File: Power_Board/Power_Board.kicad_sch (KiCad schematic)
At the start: 7 parts, among them J1 Screw_Terminal_01x02, J1_left1 Conn_01x12_Female, J1_right1 Conn_01x12_Female, J2 Conn_01x06_Female, J3 Screw_Terminal_01x02

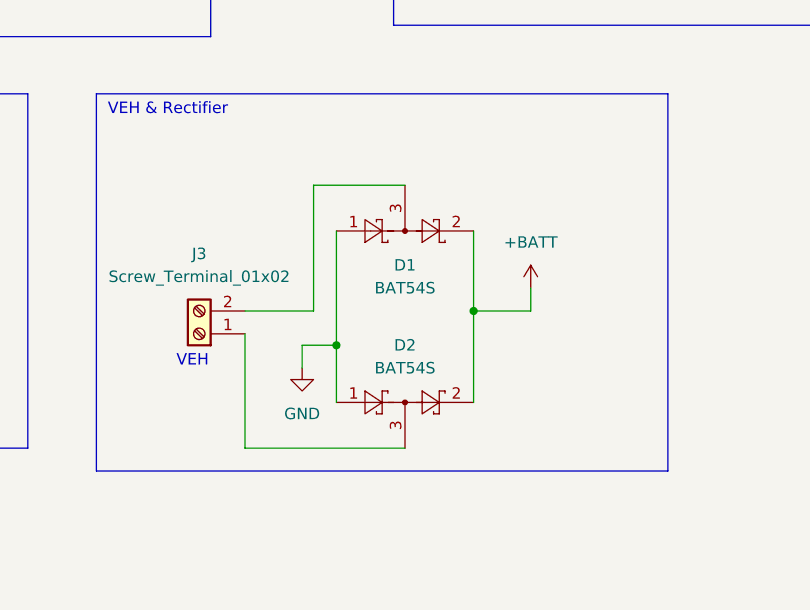
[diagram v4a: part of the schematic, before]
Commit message: Changed diod footprint
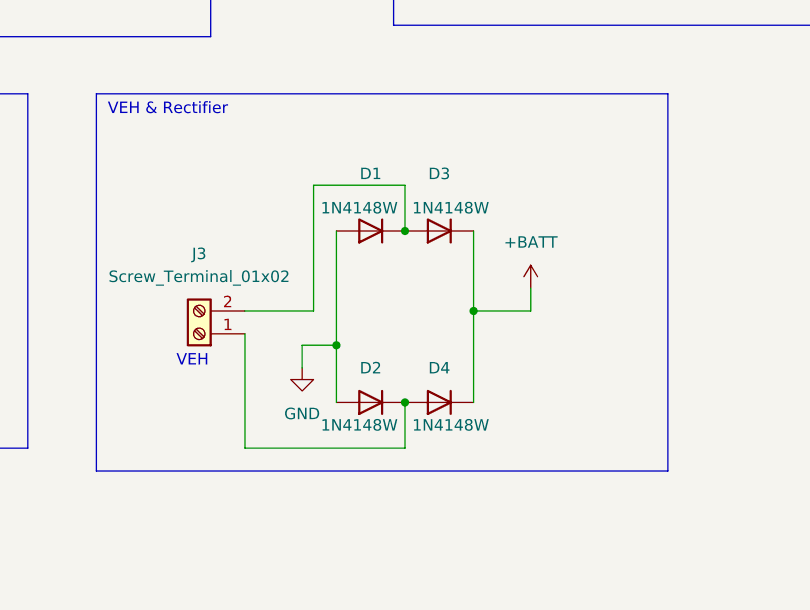
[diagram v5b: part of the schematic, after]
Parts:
- removed D1, D2: BAT54S, Package_TO_SOT_SMD:SOT-23, symbol Diode:BAT54S
- added D1, D2, D3, D4: 1N4148W, Diode_SMD:D_SOD-123, symbol Diode:1N4148W
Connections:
- net +BATT: now also D3.1 (K), D4.1 (K)
- net GND: now also D1.2 (A), D2.2 (A)
- net at J3.1 (Pin_1): now also D2.1 (K), D4.2 (A)
- net at J3.2 (Pin_2): now also D1.1 (K), D3.2 (A)
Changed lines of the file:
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@@
   (junction (at 105.41 105.41) (diameter 0) (color 0 0 0 0)
   )
+  (junction (at 113.03 111.76) (diameter 0) (color 0 0 0 0)
+  )
+  (junction (at 113.03 92.71) (diameter 0) (color 0 0 0 0)
+  )
   (wire (pts (xy 95.25 101.6) (xy 102.87 101.6))
     (stroke (width 0) (type default) (color 0 0 0 0))
@@
     (stroke (width 0) (type default) (color 0 0 0 0))
   )
+  (wire (pts (xy 113.03 111.76) (xy 113.03 116.84))
+    (stroke (width 0) (type default) (color 0 0 0 0))
+  )
   (wire (pts (xy 142.24 41.91) (xy 142.24 34.29))
+    (stroke (width 0) (type default) (color 0 0 0 0))
+  )
+  (wire (pts (xy 113.03 87.63) (xy 113.03 92.71))
     (stroke (width 0) (type default) (color 0 0 0 0))
   )
@@
     (pin "1")
   )
+  (symbol (lib_id "Diode:1N4148W") (at 116.84 92.71 180) (unit 1)
+    (in_bom yes) (on_board yes)
+    (property "Reference" "D3" (id 0) (at 116.84 86.36 0))
+    (property "Value" "1N4148W" (id 1) (at 118.11 90.17 0))
+    (property "Footprint" "Diode_SMD:D_SOD-123" (id 2) (at 116.84 88.265 0)
+      (effects (font (size 1.27 1.27)) hide)
+    )
+    (property "Datasheet" "https://www.vishay.com/docs/85748/1n4148w.pdf" (id 3) (at 116.84 92.71 0)
+      (effects (font (size 1.27 1.27)) hide)
+    )
+    (pin "1")
+    (pin "2")
+  )
+  (symbol (lib_id "Diode:1N4148W") (at 109.22 92.71 180) (unit 1)
+    (in_bom yes) (on_board yes)
+    (property "Reference" "D1" (id 0) (at 109.22 86.36 0))
+    (property "Value" "1N4148W" (id 1) (at 107.95 90.17 0))
+    (property "Footprint" "Diode_SMD:D_SOD-123" (id 2) (at 109.22 88.265 0)
+      (effects (font (size 1.27 1.27)) hide)
+    )
+    (property "Datasheet" "https://www.vishay.com/docs/85748/1n4148w.pdf" (id 3) (at 109.22 92.71 0)
+      (effects (font (size 1.27 1.27)) hide)
+    )
+    (pin "1")
+    (pin "2")
+  )
   (symbol (lib_id "power:+3V3") (at 279.4 124.46 0) (unit 1)
     (in_bom yes) (on_board yes) (fields_autoplaced)
@@
     )
     (pin "1")
-  )
-  (symbol (lib_id "Diode:BAT54S") (at 113.03 111.76 0) (unit 1)
-    (in_bom yes) (on_board yes)
-    (property "Reference" "D2" (id 0) (at 113.03 105.41 0))
-    (property "Value" "BAT54S" (id 1) (at 113.03 107.95 0))
-    (property "Footprint" "Package_TO_SOT_SMD:SOT-23" (id 2) (at 114.935 108.585 0)
-      (effects (font (size 1.27 1.27)) (justify left) hide)
-    )
-    (property "Datasheet" "https://www.diodes.com/assets/Datasheets/ds11005.pdf" (id 3) (at 109.982 111.76 0)
-      (effects (font (size 1.27 1.27)) hide)
-    )
-    (pin "1")
-    (pin "2")
-    (pin "3")
   )
   (symbol (lib_id "Connector:Conn_01x12_Female") (at 72.39 45.72 0) (mirror y) (unit 1)
@@
     (pin "2")
   )
+  (symbol (lib_id "Diode:1N4148W") (at 116.84 111.76 180) (unit 1)
+    (in_bom yes) (on_board yes)
+    (property "Reference" "D4" (id 0) (at 116.84 107.95 0))
+    (property "Value" "1N4148W" (id 1) (at 118.11 114.3 0))
+    (property "Footprint" "Diode_SMD:D_SOD-123" (id 2) (at 116.84 107.315 0)
+      (effects (font (size 1.27 1.27)) hide)
+    )
+    (property "Datasheet" "https://www.vishay.com/docs/85748/1n4148w.pdf" (id 3) (at 116.84 111.76 0)
+      (effects (font (size 1.27 1.27)) hide)
+    )
+    (pin "1")
+    (pin "2")
+  )
   (symbol (lib_id "power:+BATT") (at 265.43 82.55 0) (unit 1)
     (in_bom yes) (on_board yes) (fields_autoplaced)
@@
     (pin "1")
   )
-  (symbol (lib_id "Diode:BAT54S") (at 113.03 92.71 0) (mirror x) (unit 1)
-    (in_bom yes) (on_board yes) (fields_autoplaced)
-    (property "Reference" "D1" (id 0) (at 113.03 96.52 0))
-    (property "Value" "BAT54S" (id 1) (at 113.03 99.06 0))
-    (property "Footprint" "Package_TO_SOT_SMD:SOT-23" (id 2) (at 114.935 95.885 0)
-      (effects (font (size 1.27 1.27)) (justify left) hide)
-    )
-    (property "Datasheet" "https://www.diodes.com/assets/Datasheets/ds11005.pdf" (id 3) (at 109.982 92.71 0)
-      (effects (font (size 1.27 1.27)) hide)
-    )
-    (pin "1")
-    (pin "2")
-    (pin "3")
-  )
   (symbol (lib_id "power:+BATT") (at 127 99.06 0) (unit 1)
     (in_bom yes) (on_board yes) (fields_autoplaced)
@@
     (pin "6")
   )
+  (symbol (lib_id "Diode:1N4148W") (at 109.22 111.76 180) (unit 1)
+    (in_bom yes) (on_board yes)
+    (property "Reference" "D2" (id 0) (at 109.22 107.95 0))
+    (property "Value" "1N4148W" (id 1) (at 107.95 114.3 0))
+    (property "Footprint" "Diode_SMD:D_SOD-123" (id 2) (at 109.22 107.315 0)
+      (effects (font (size 1.27 1.27)) hide)
+    )
+    (property "Datasheet" "https://www.vishay.com/docs/85748/1n4148w.pdf" (id 3) (at 109.22 111.76 0)
+      (effects (font (size 1.27 1.27)) hide)
+    )
+    (pin "1")
+    (pin "2")
+  )
   (sheet_instances
     (path "/" (page "1"))
@@
       (reference "#PWR0108") (unit 1) (value "+BATT") (footprint "")
     )
-    (path "/d1ceb342-998d-4c5b-ad19-ab664694b8dd"
-      (reference "D1") (unit 1) (value "BAT54S") (footprint "Package_TO_SOT_SMD:SOT-23")
-    )
-    (path "/4dba1e97-eac0-407d-81c2-57ef7f9dc24d"
-      (reference "D2") (unit 1) (value "BAT54S") (footprint "Package_TO_SOT_SMD:SOT-23")
+    (path "/415ab9a2-305a-41f0-b1db-7c916ad678f7"
+      (reference "D1") (unit 1) (value "1N4148W") (footprint "Diode_SMD:D_SOD-123")
+    )
+    (path "/f9c5d929-bc41-466c-9057-315ad1333942"
+      (reference "D2") (unit 1) (value "1N4148W") (footprint "Diode_SMD:D_SOD-123")
+    )
+    (path "/268b6f70-8ec4-4324-b612-153578d7a932"
+      (reference "D3") (unit 1) (value "1N4148W") (footprint "Diode_SMD:D_SOD-123")
+    )
+    (path "/7ab1291c-0671-47a2-869a-f7c35e58ac55"
+      (reference "D4") (unit 1) (value "1N4148W") (footprint "Diode_SMD:D_SOD-123")
     )
     (path "/7059482a-1ab5-41af-a31c-5533b284b340"

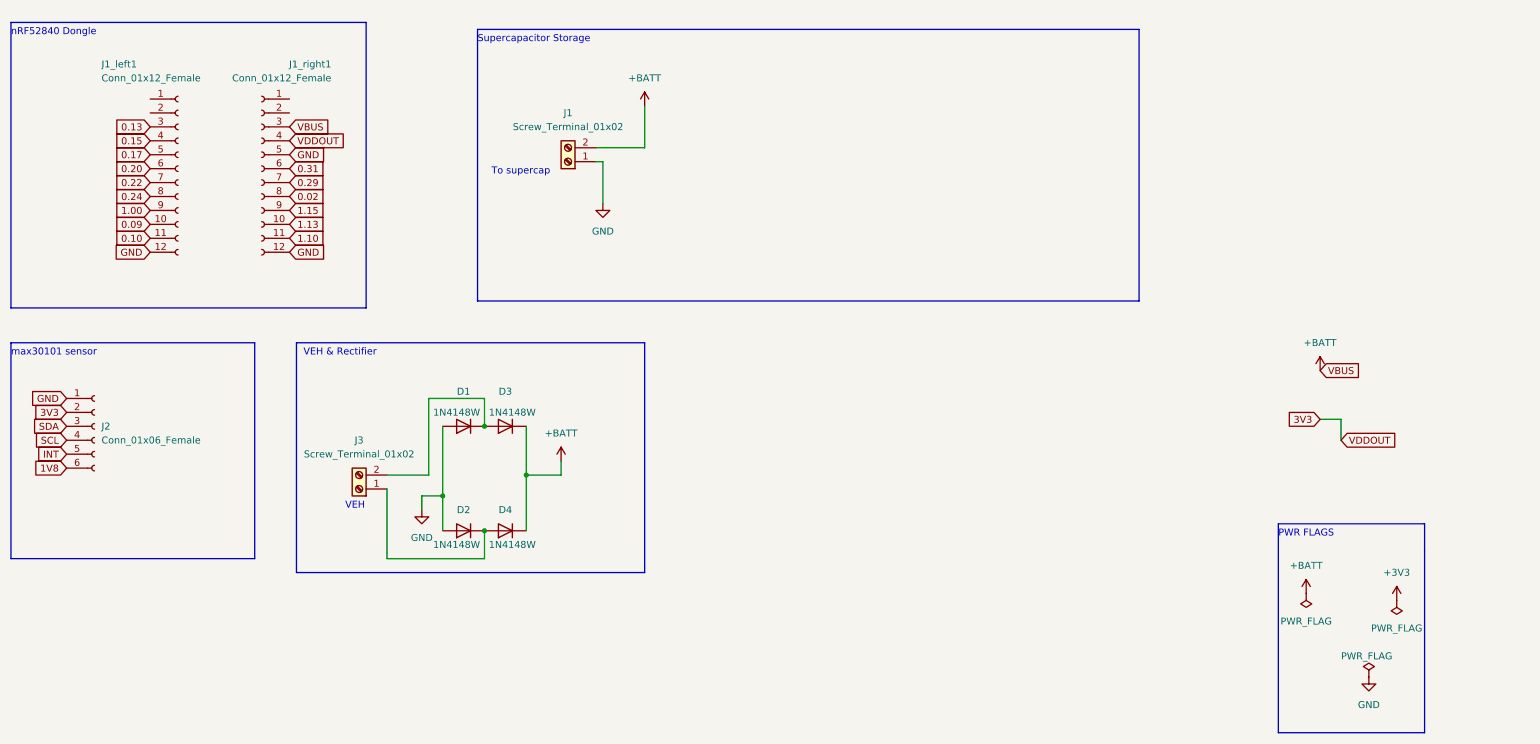
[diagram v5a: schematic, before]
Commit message: voltage regulator added
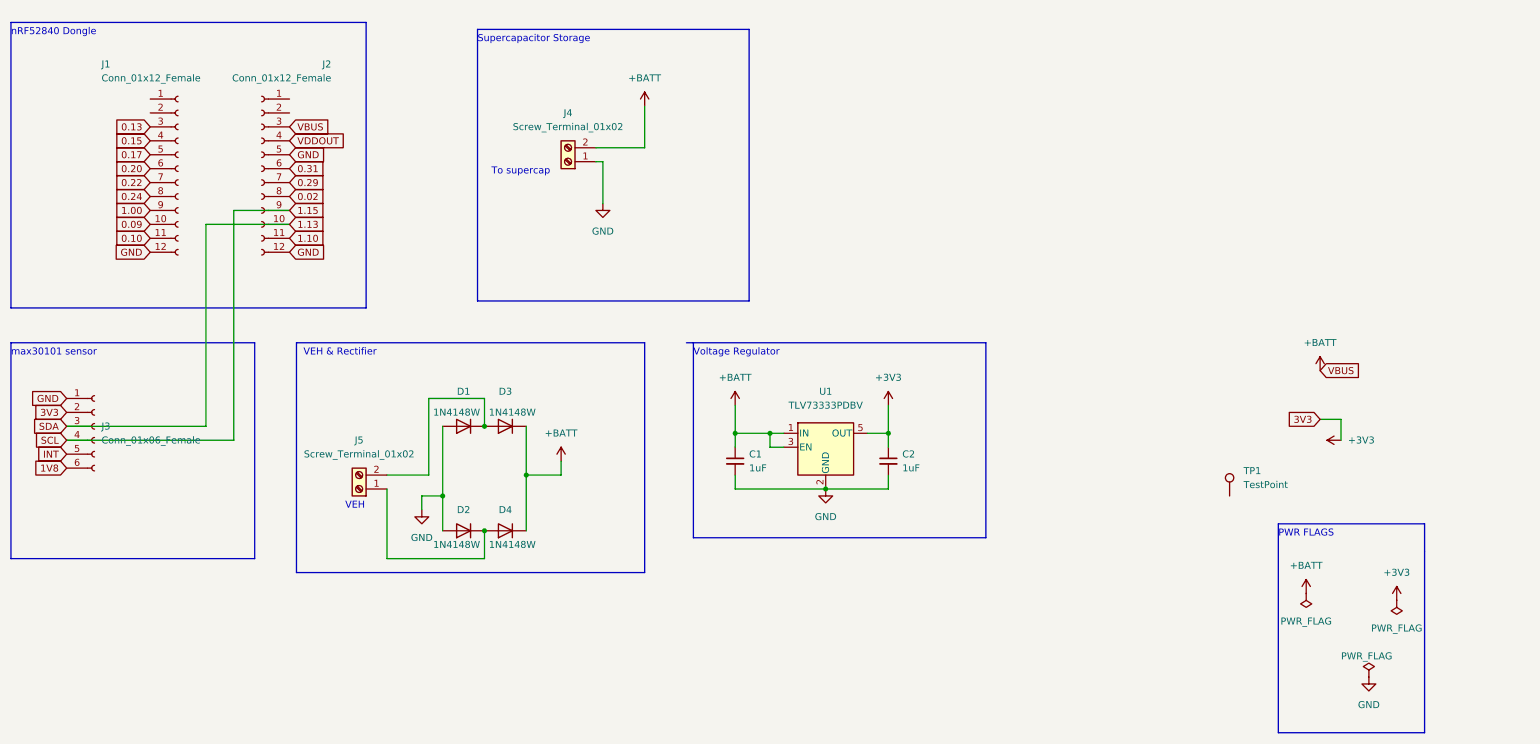
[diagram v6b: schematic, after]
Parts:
- added C1, C2: 1uF, Capacitor_SMD:C_0201_0603Metric, symbol Device:C_Small
- added TP1: TestPoint, symbol Connector:TestPoint
- added U1: TLV73333PDBV, Package_TO_SOT_SMD:SOT-23-5, symbol Regulator_Linear:TLV73333PDBV
- renumbered J1_left1 to J1, J1_right1 to J2, J2 to J3, J1 to J4, J3 to J5
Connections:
- net SCL is gone; now on net 1.15: J3.4 (Pin_4)
- net SDA is gone; now on net 1.13: J3.3 (Pin_3)
- net +3V3: now also J3.2 (Pin_2), C2.1, U1.5 (OUT)
- net +BATT: now also C1.1, U1.1 (IN), U1.3 (EN)
- net GND: now also C1.2, C2.2, U1.2 (GND)
- net 3V3 renamed VDDOUT
- net VDDOUT: no longer J3.2 (Pin_2)
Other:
- note added: "Voltage Regulator"

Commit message: latest update with rectifier
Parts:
- removed C1, C2: 1uF, Capacitor_SMD:C_0201_0603Metric, symbol Device:C_Small
- removed D1, D2, D3, D4: 1N4148W, Diode_SMD:D_SOD-123, symbol Diode:1N4148W
- removed J1, J2: Conn_01x12_Female, Connector_PinSocket_2.54mm:PinSocket_1x12_P2.54mm_Vertical, symbol Connector:Conn_01x12_Female
- removed U1: TLV73333PDBV, Package_TO_SOT_SMD:SOT-23-5, symbol Regulator_Linear:TLV73333PDBV
- added D1, D2: BAT54S, Package_TO_SOT_SMD:SOT-23, symbol Diode:BAT54S
- added J1, J2: Conn_01x10_Female, Connector_PinSocket_2.54mm:PinSocket_1x10_P2.54mm_Vertical, symbol Connector:Conn_01x10_Female
- added TP2: VEH_2, Connector_Pin:Pin_D1.0mm_L10.0mm, symbol Connector:TestPoint
- added TP3: VEH_OUT, Connector_Pin:Pin_D1.0mm_L10.0mm, symbol Connector:TestPoint
- TP1: value TestPoint -> VEH_1; footprint (none) -> Connector_Pin:Pin_D1.0mm_L10.0mm
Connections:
- net +BATT: now also D1.2, D2.2, J2.1 (Pin_1), TP3.1
- net 0.02: now also J2.6 (Pin_6)
- net 0.09: now also J1.8 (Pin_8)
- net 0.10: now also J1.9 (Pin_9)
- net 0.13: now also J1.1 (Pin_1)
- net 0.15: now also J1.2 (Pin_2)
- net 0.17: now also J1.3 (Pin_3)
- net 0.20: now also J1.4 (Pin_4)
- net 0.22: now also J1.5 (Pin_5)
- net 0.24: now also J1.6 (Pin_6)
- net 0.29: now also J2.5 (Pin_5)
- net 0.31: now also J2.4 (Pin_4)
- net 1.00: now also J1.7 (Pin_7)
- net 1.10: now also J2.9 (Pin_9)
- net 1.13: now also J3.4 (Pin_4), J2.8 (Pin_8); no longer J3.3 (Pin_3)
- net 1.15: now also J3.3 (Pin_3), J2.7 (Pin_7); no longer J3.4 (Pin_4)
- net GND: now also D1.1, D2.1, J1.10 (Pin_10), J2.10 (Pin_10), J2.3 (Pin_3)
- net at J5.2 (Pin_2): now also TP1.1, D1.3
- net at J5.1 (Pin_1): now also D2.3, TP2.1
- net +3V3 renamed 3V3
- net 3V3: now also J2.2 (Pin_2)
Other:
- note added: "Thing to do: 1) connect dongle with sensor 2) add pads for dongle 3) add TPs"
- note added: "VEH input"
- note removed: "VEH"
- note removed: "Voltage Regulator"

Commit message: PCB layout update
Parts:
- added H1: MountingHole, symbol Mechanical:MountingHole
- added H2, H3, H4: MountingHole, MountingHole:MountingHole_2.2mm_M2, symbol Mechanical:MountingHole
- added TP4: VDDOUT, TestPoint:TestPoint_Pad_D1.5mm, symbol Connector:TestPoint
- added TP5: 1.15, TestPoint:TestPoint_Pad_D1.5mm, symbol Connector:TestPoint
- added TP6: 1.13, TestPoint:TestPoint_Pad_D1.5mm, symbol Connector:TestPoint
- added TP7, TP9: GND, TestPoint:TestPoint_Pad_D1.5mm, symbol Connector:TestPoint
- added TP8: C+, TestPoint:TestPoint_Pad_D1.5mm, symbol Connector:TestPoint
- TP1, TP2, TP3: footprint Connector_Pin:Pin_D1.0mm_L10.0mm -> TestPoint:TestPoint_Pad_D1.5mm
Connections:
- net +BATT: now also TP8.1
- net 1.13: now also TP6.1
- net 1.15: now also TP5.1
- net 3V3: now also TP4.1
- net GND: now also TP7.1, TP9.1
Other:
- note added: "Mounting Holes"
- note added: "The castellated edge holes have a pitch of 0.1 inches (2.54 mm) and a row spacing of 0.6 inches (15.24 mm)2, making it suitable for stripboard connection. The SWD connections are located 0.2 inches (5.08 mm) away from the GPIOs with a row spacing of 0.4 inches (10.16 mm)"
